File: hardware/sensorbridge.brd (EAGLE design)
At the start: 17 x 11.2 mm, 19 parts, among them X1 1503_11, X2 1503_11, X3 1503_11, X4 1503_11, X5 1503_11, X6 1503_11

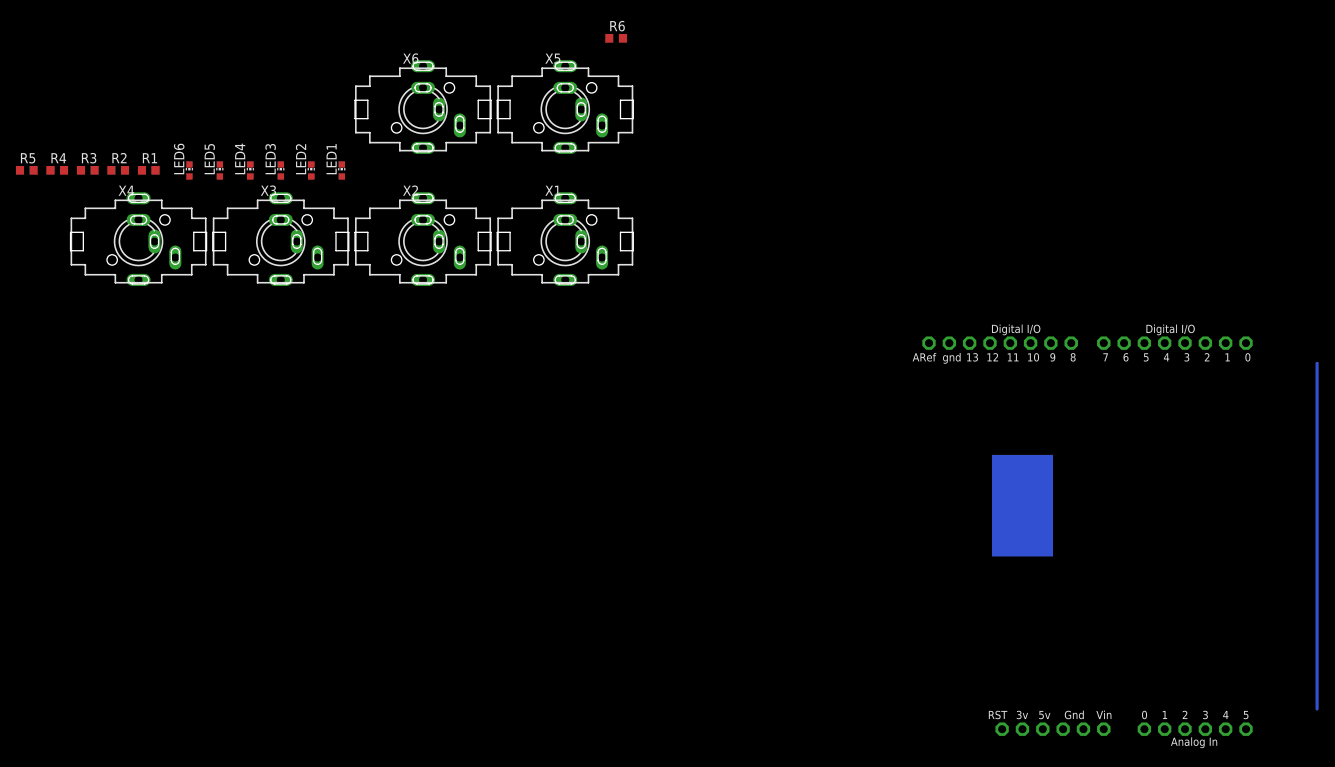
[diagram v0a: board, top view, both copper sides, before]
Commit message: Updated board layout, replaced jack, added status led
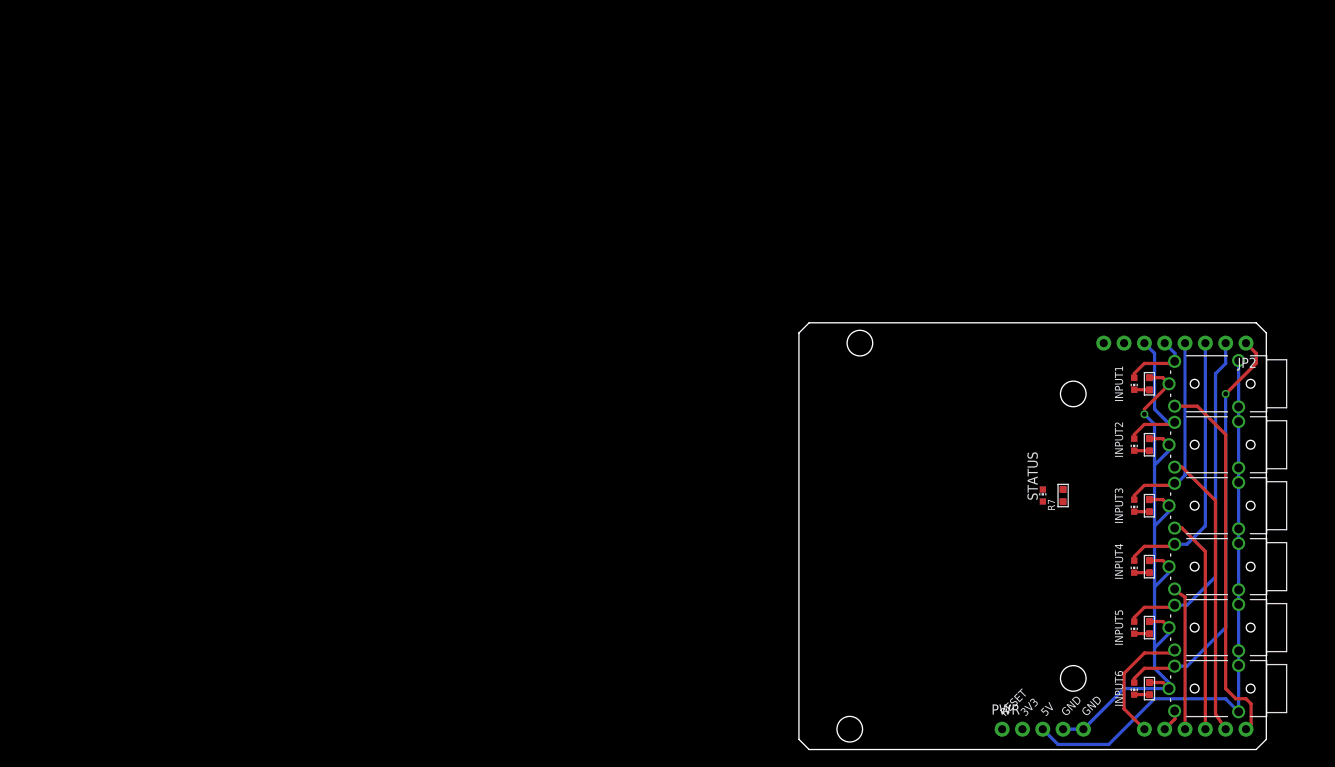
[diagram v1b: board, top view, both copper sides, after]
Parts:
- removed U$2: ARDUINO-NOHOLE, adafruit:ARDUINO-NOHOLE
- removed X1, X2, X3, X4, X5, X6: 1503_11, con-lumberg:1503_11
- added ANALOG: (no value), SparkFun-Connectors:1X06_NO_SILK
- added INPUT1, INPUT2, INPUT3, INPUT4, INPUT5, INPUT6: MJ-2135, sensorlab:MJ-2135
- added JP2: (no value), SparkFun-Connectors:1X08_NO_SILK
- added PWR: (no value), SparkFun-Connectors:1X05_NO_SILK
- added R7: (no value), Seeed-OPL-Resistor:R0603
- added STATUS: (no value), adafruit:CHIP-LED0603
- R1, R2, R3, R4, R5, R6: device adafruit:R0603 -> Seeed-OPL-Resistor:R0603
- moved R5 151.5 mm to (51.4, 15.2)
- moved R4 145.2 mm to (51.4, 22.9)
- moved R3 139.2 mm to (51.4, 30.5)
- moved LED6 134.7 mm to (49.5, 7.62), turned to 180 degrees
- moved R2 133.4 mm to (51.4, 38.1)
- moved R1 127.9 mm to (51.4, 45.7)
- moved LED5 127.8 mm to (49.5, 15.2), turned to 180 degrees
- moved LED4 121.1 mm to (49.5, 22.9), turned to 180 degrees
- moved LED3 114.6 mm to (49.5, 30.5), turned to 180 degrees
- moved LED2 108.4 mm to (49.5, 38.1), turned to 180 degrees
- moved R6 105.1 mm to (51.4, 7.62)
- moved LED1 102.6 mm to (49.5, 45.7), turned to 180 degrees
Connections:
- removed net 5V: U$2.5V
- removed net A0: U$2.A0
- removed net D0: U$2.D0
- removed net GND1: U$2.GND1
- removed net GND2: U$2.GND2
- removed net VIN: U$2.VIN
- new net N$7: R7.2, STATUS.C
- new net N$8: JP2.7, STATUS.A
- new net RESET: PWR.1
- net +5V: now also INPUT1.4, INPUT1.4@2, INPUT2.4, INPUT2.4@2, INPUT3.4, INPUT3.4@2, INPUT4.4, INPUT4.4@2, INPUT5.4, INPUT5.4@2, INPUT6.4, INPUT6.4@2, PWR.3; no longer X1.3, X2.3, X3.3, X4.3, X5.3, X6.3
- net 3V: now also PWR.2; no longer U$2.3V
- net GND: now also INPUT1.1, INPUT2.1, INPUT3.1, INPUT4.1, INPUT5.1, INPUT6.1, PWR.4, PWR.5, R7.1; no longer U$2.GND, X1.1, X2.1, X3.1, X4.1, X5.1, X6.1
- net S1_CONN: now also INPUT1.3, JP2.5; no longer X2.4, X2.5
- net S1_DATA: now also ANALOG.6, INPUT1.2; no longer X2.2
- net S2_CONN: now also INPUT2.3, JP2.6; no longer X1.4, X1.5
- net S2_DATA: now also ANALOG.5, INPUT2.2; no longer X1.2
- net S3_CONN: now also INPUT3.3, JP2.4; no longer X3.4, X3.5
- net S3_DATA: now also ANALOG.4, INPUT3.2; no longer X3.2
- net S4_CONN: now also INPUT4.3, JP2.3; no longer X4.4, X4.5
- net S4_DATA: now also ANALOG.3, INPUT4.2; no longer X4.2
- net S5_CONN: now also INPUT5.3, JP2.2; no longer X5.4, X5.5
- net S5_DATA: now also ANALOG.1, INPUT5.2; no longer X5.2
- net S6_CONN: now also INPUT6.3, JP2.1; no longer X6.4, X6.5
- net S6_DATA: now also ANALOG.2, INPUT6.2; no longer X6.2
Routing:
- net GND: track 0.00 -> 86.0 mm, vias 0 -> 1
- net +5V: track 0.00 -> 72.2 mm
- net S6_CONN: track 0.00 -> 52.2 mm, vias 0 -> 1
- net S1_DATA: track 0.00 -> 47.0 mm
- net N$7: track 43.2 -> 0.00 mm
- net S5_CONN: track 0.00 -> 42.5 mm
- net S2_DATA: track 0.00 -> 35.8 mm
- net S4_CONN: track 0.00 -> 33.8 mm
- net S3_DATA: track 0.00 -> 27.3 mm
- net S3_CONN: track 0.00 -> 24.4 mm
- net S2_CONN: track 0.00 -> 19.0 mm
- net S4_DATA: track 0.00 -> 18.2 mm
- net S5_DATA: track 0.00 -> 15.6 mm
- net S1_CONN: track 0.00 -> 9.02 mm
- net S6_DATA: track 0.00 -> 2.81 mm
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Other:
- board size 17 x 11.2 mm -> 58.4 x 53.3 mm
- board text added: "3V3"
- board text added: "5V"
- board text added: "GND"
- board text added: "RESET"

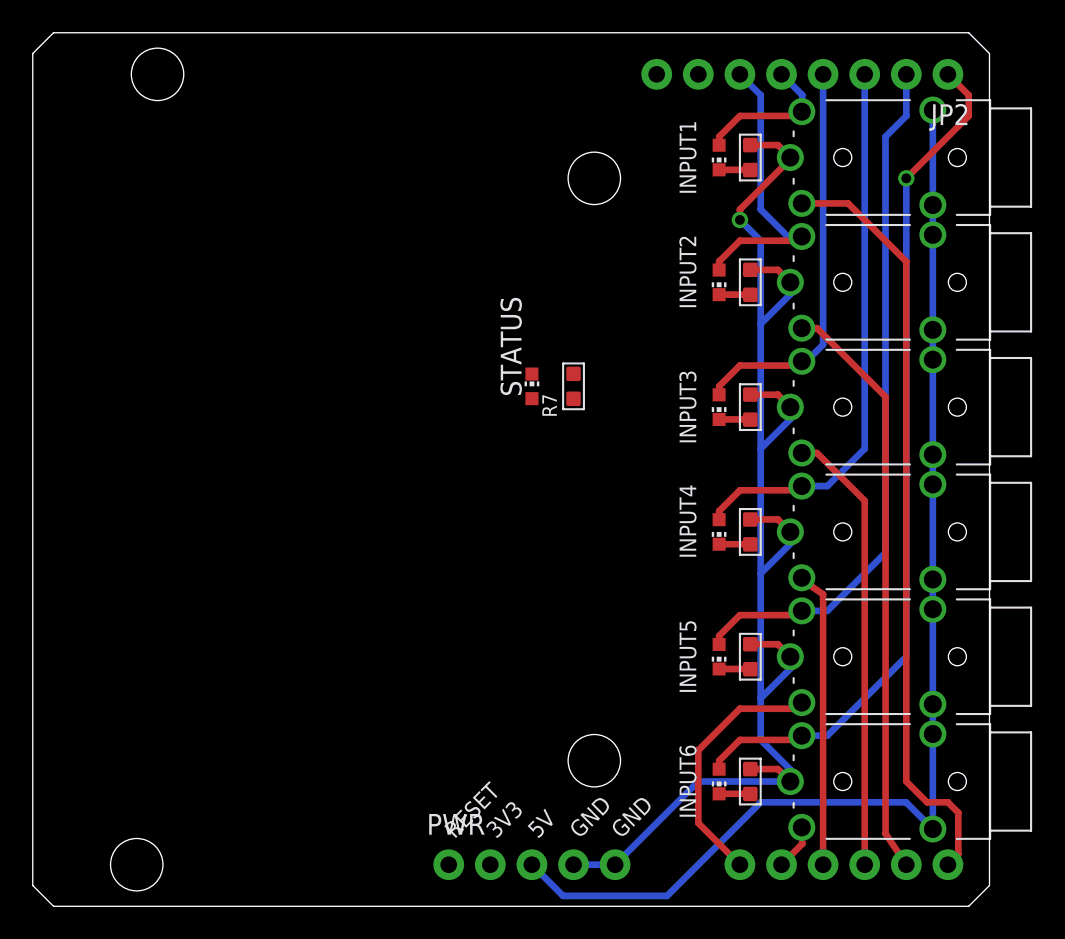
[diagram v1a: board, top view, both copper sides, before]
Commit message: Adapted shield outline
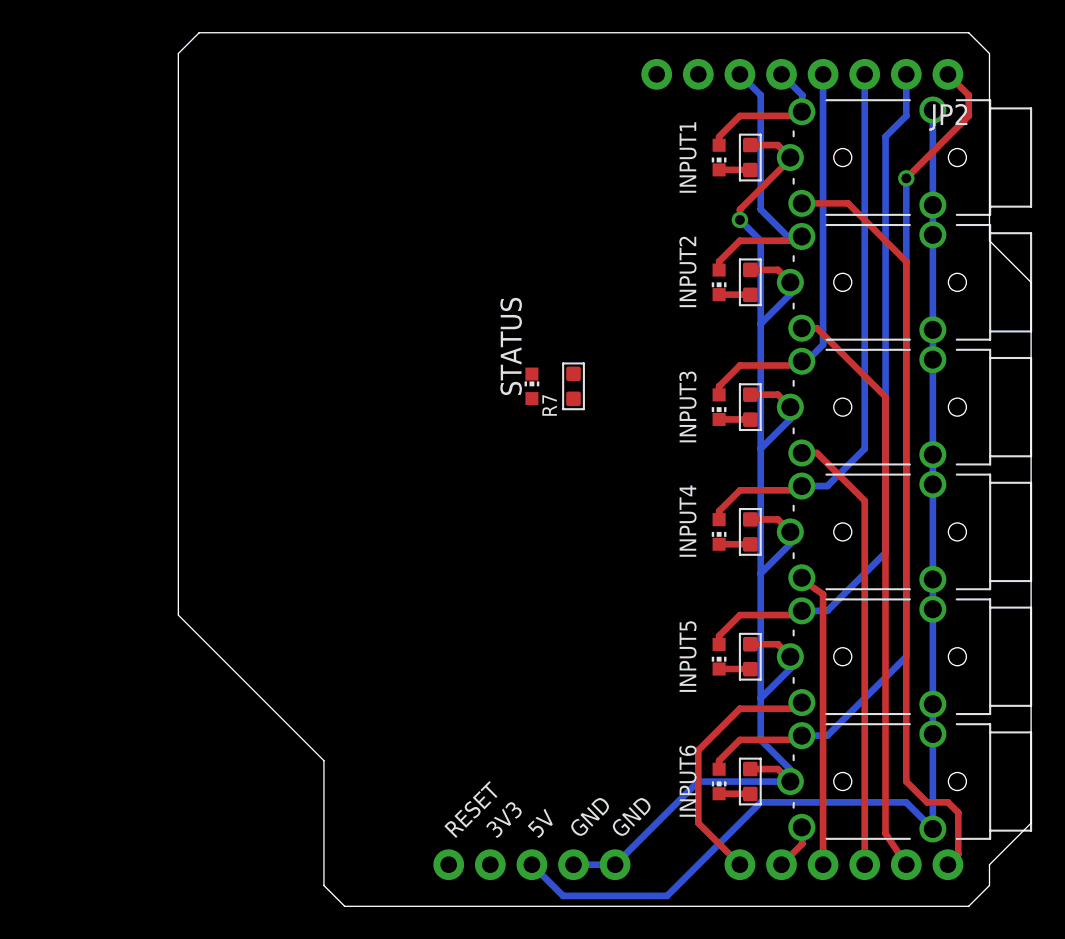
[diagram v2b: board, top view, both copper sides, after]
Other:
- board size 58.4 x 53.3 mm -> 52.1 x 53.3 mm

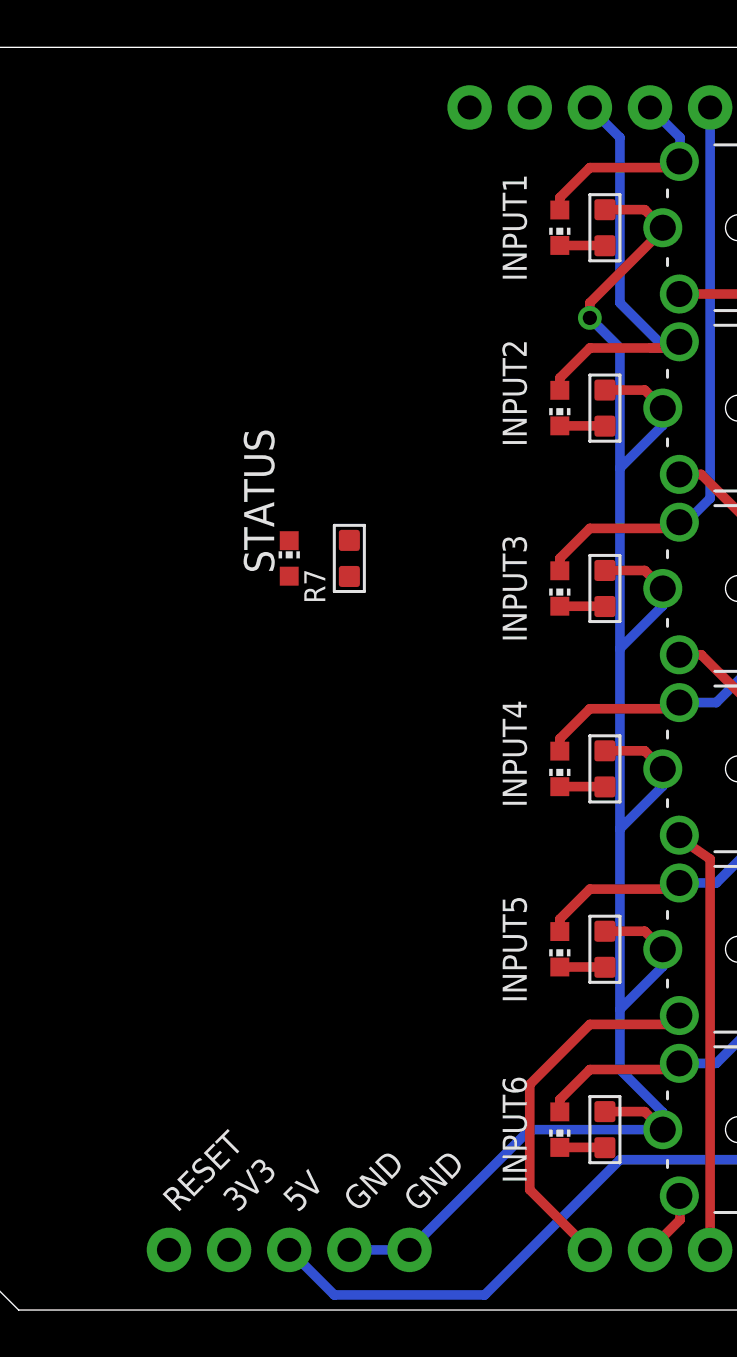
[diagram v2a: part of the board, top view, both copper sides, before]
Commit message: Added power led
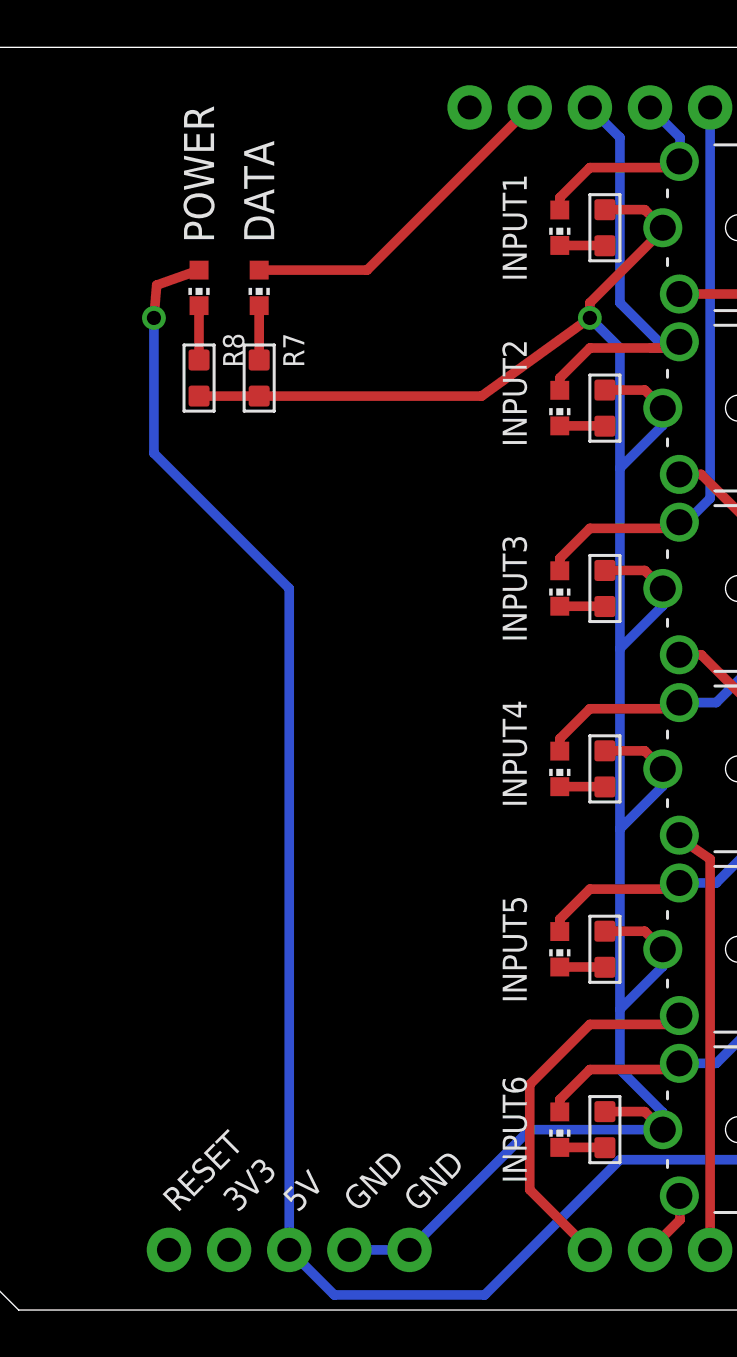
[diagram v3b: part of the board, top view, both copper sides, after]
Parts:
- removed STATUS: (no value), adafruit:CHIP-LED0603
- added DATA, POWER: (no value), adafruit:CHIP-LED0603
- added R8: (no value), Seeed-OPL-Resistor:R0603
- moved R7 8.52 mm to (36.8, 39.4), turned to 180 degrees
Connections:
- new net N$9: POWER.C, R8.2
- net +5V: now also POWER.A
- net GND: now also R8.1
- net N$7: now also DATA.C; no longer STATUS.C
- net N$8: now also DATA.A; no longer STATUS.A
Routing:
- net +5V: track 72.2 -> 117.2 mm, vias 0 -> 1
- net GND: track 86.0 -> 103.6 mm
- net N$8: track 0.00 -> 14.3 mm
- net N$9: track 0.00 -> 2.30 mm
- net N$7: track 0.00 -> 2.30 mm

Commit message: Added arduino pin names to info layer
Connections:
- new net N$10: JP2.8
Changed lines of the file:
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@@
 <wire x1="34.29" y1="42.43" x2="34.29" y2="40.132" width="0.4064" layer="1"/>
+</signal>
+<signal name="N$10">
+<contactref element="JP2" pad="8"/>
 </signal>
 </signals>

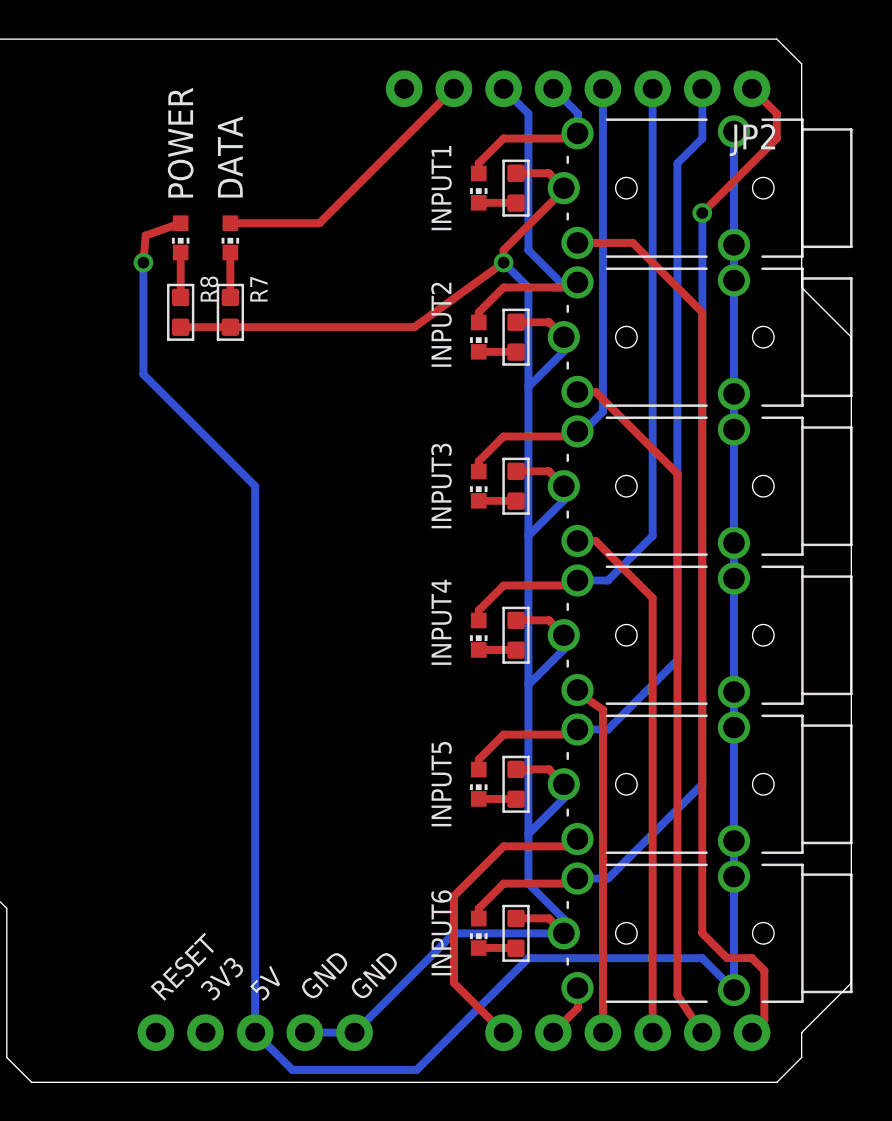
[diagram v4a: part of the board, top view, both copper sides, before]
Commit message: Digital pin reconfiguration
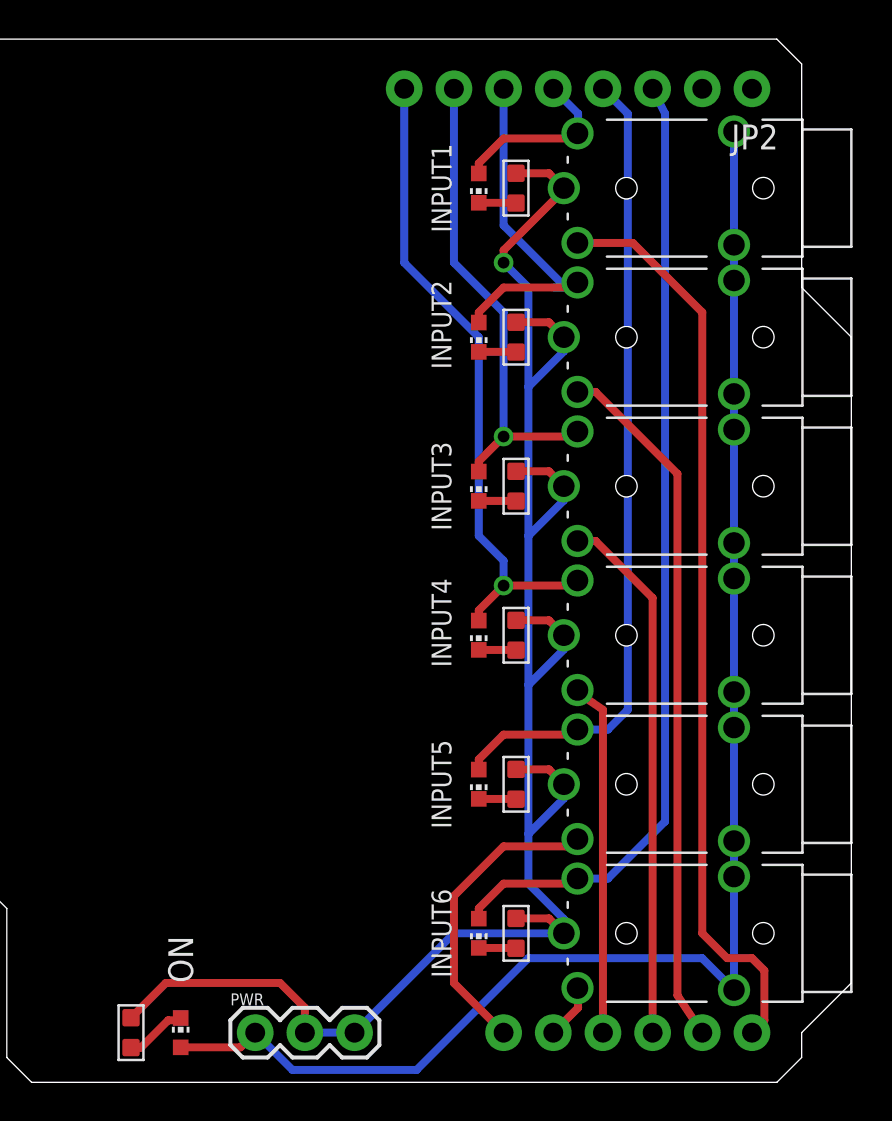
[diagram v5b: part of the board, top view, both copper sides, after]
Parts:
- removed DATA, POWER: (no value), adafruit:CHIP-LED0603
- removed R7: (no value), Seeed-OPL-Resistor:R0603
- added ON: (no value), adafruit:CHIP-LED0603
- PWR: device SparkFun-Connectors:1X05_NO_SILK -> SparkFun-Connectors:1X03
- moved R8 36.9 mm to (31.8, 2.54), turned to 0 degrees
- moved PWR 5.08 mm to (38.1, 2.54)
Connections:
- removed net 3V: PWR.2
- removed net N$10: JP2.8
- removed net N$7: DATA.C, R7.2
- removed net N$8: DATA.A, JP2.7
- removed net RESET: PWR.1
- new net N$12: JP2.2
- new net N$13: JP2.1
- net +5V: now also ON.A, PWR.1; no longer POWER.A, PWR.3
- net GND: now also PWR.2, PWR.3; no longer PWR.4, PWR.5, R7.1
- net N$9: now also ON.C; no longer POWER.C
- net S3_CONN: now also JP2.7; no longer JP2.4
- net S4_CONN: now also JP2.8; no longer JP2.3
- net S5_CONN: now also JP2.4; no longer JP2.2
- net S6_CONN: now also JP2.3; no longer JP2.1
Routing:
- net +5V: track 117.2 -> 76.3 mm, vias 1 -> 0
- net N$8: track 14.3 -> 0.00 mm
- net GND: track 103.6 -> 97.5 mm
- net S6_CONN: track 52.2 -> 49.5 mm, vias 1 -> 0
- net N$7: track 2.30 -> 0.00 mm
- net S5_CONN: track 42.5 -> 41.5 mm
- net N$9: track 2.30 -> 3.17 mm
- net S3_CONN: track 24.4 -> 25.0 mm, vias 0 -> 1
- net S4_CONN: track 33.8 -> 33.7 mm, vias 0 -> 1
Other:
- board text removed: "3V3"
- board text removed: "5V"
- board text removed: "GND"
- board text removed: "RESET"
